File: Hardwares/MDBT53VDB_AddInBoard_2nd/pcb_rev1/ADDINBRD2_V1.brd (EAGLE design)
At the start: 25 x 31 mm, 21 parts, among them CN1 IF_4PIN, CN2 IF_4PIN, CN3 IF_2PIN, CN4 IF_2PIN, Q1 DMP2035UFDF-7, Q2 BC817-40QA, SW1 SKRPACE010, U1 SN74AHC1G00DRLR, U2 REF3325AIRSER, U3 MCP6232T-E/MNY

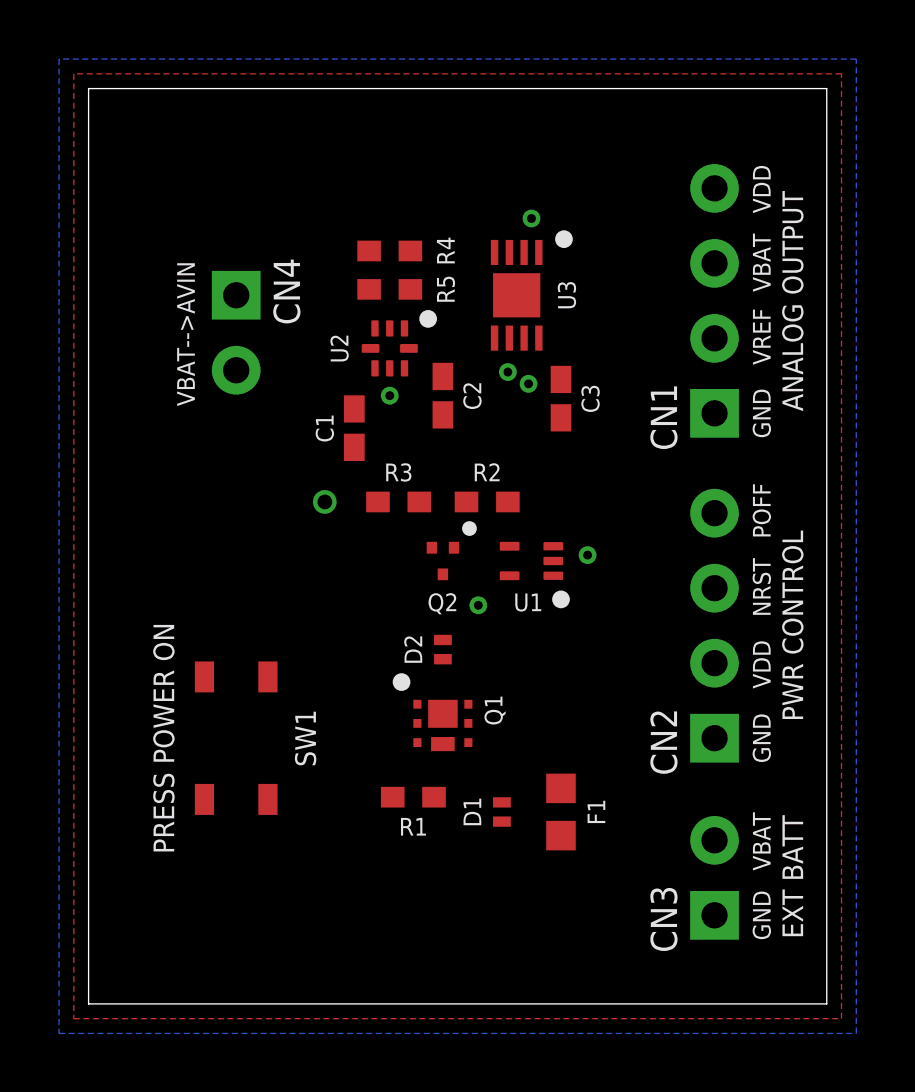
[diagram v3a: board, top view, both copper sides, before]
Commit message: レイアウトを修正
・MOSFET周りを配線
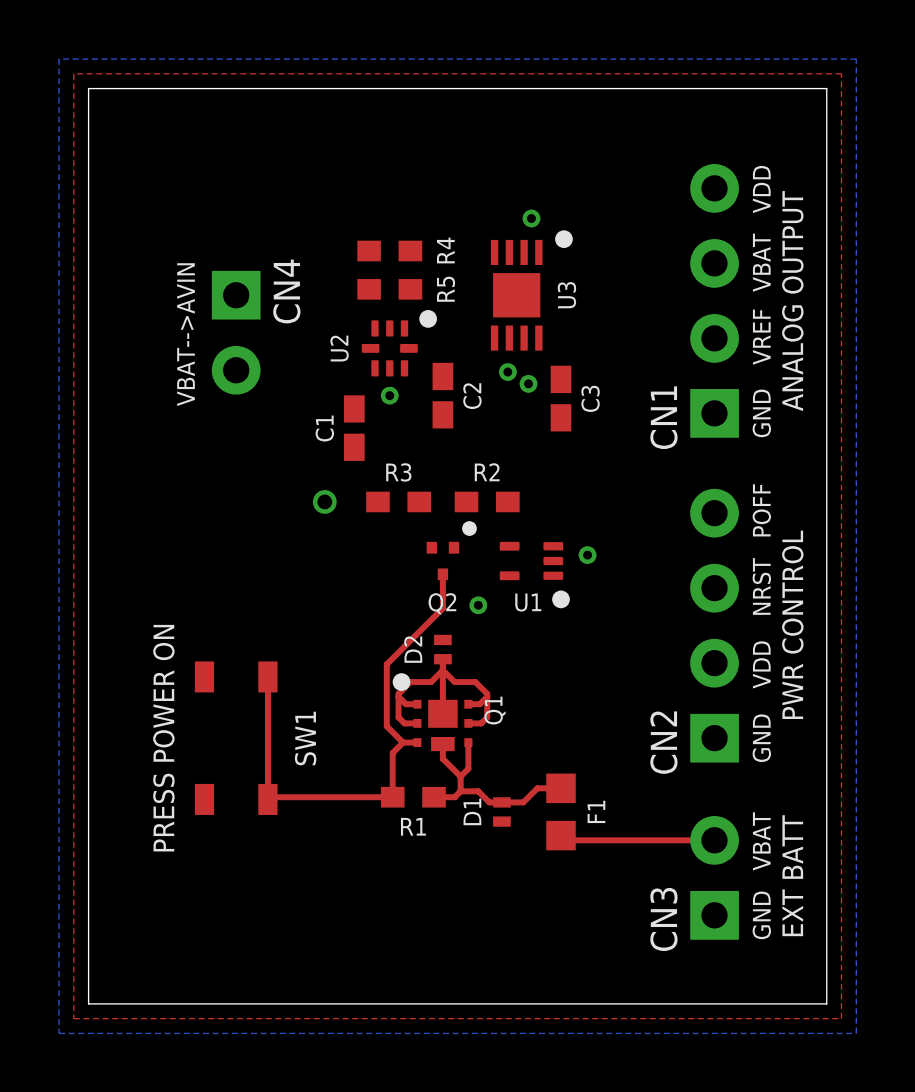
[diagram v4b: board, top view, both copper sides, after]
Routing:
- net PWR_G: track 0.00 -> 17.6 mm
- net N$2: track 0.00 -> 10.4 mm
- net N$1: track 0.00 -> 7.84 mm
- net EXT_BAT: track 0.00 -> 5.27 mm
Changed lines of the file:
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@@
 <contactref element="Q1" pad="EXP2"/>
 <contactref element="Q1" pad="4"/>
-<wire x1="14" y1="6.825" x2="16" y2="7.3" width="0" layer="19" extent="1-1"/>
-<wire x1="12.863" y1="8.85" x2="14" y2="6.825" width="0" layer="19" extent="1-1"/>
-<wire x1="12" y1="8.8" x2="12.863" y2="8.85" width="0" layer="19" extent="1-1"/>
-<wire x1="11.7" y1="7" x2="12" y2="8.8" width="0" layer="19" extent="1-1"/>
+<wire x1="14" y1="6.825" x2="14.725" y2="6.825" width="0.2032" layer="1"/>
+<wire x1="14.725" y1="6.825" x2="15.2" y2="7.3" width="0.2032" layer="1"/>
+<wire x1="16" y1="7.3" x2="15.2" y2="7.3" width="0.2032" layer="1"/>
+<wire x1="14" y1="6.825" x2="13.575" y2="6.825" width="0.2032" layer="1"/>
+<wire x1="12" y1="8.8" x2="12" y2="8.3" width="0.2032" layer="1"/>
+<wire x1="13.575" y1="6.825" x2="13.2" y2="7.2" width="0.2032" layer="1"/>
+<wire x1="13.2" y1="7.2" x2="12.6" y2="7.2" width="0.2032" layer="1"/>
+<wire x1="12.6" y1="7.2" x2="12.4" y2="7" width="0.2032" layer="1"/>
+<wire x1="12.4" y1="7" x2="11.7" y2="7" width="0.2032" layer="1"/>
+<wire x1="12" y1="8.3" x2="12.6" y2="7.7" width="0.2032" layer="1"/>
+<wire x1="12.6" y1="7.7" x2="12.6" y2="7.2" width="0.2032" layer="1"/>
+<wire x1="12.863" y1="8.85" x2="12.863" y2="7.963" width="0.2032" layer="1"/>
+<wire x1="12.863" y1="7.963" x2="12.6" y2="7.7" width="0.2032" layer="1"/>
 </signal>
 <signal name="PWR_G">
@@
 <contactref element="Q2" pad="3"/>
 <contactref element="Q1" pad="3"/>
-<wire x1="11.137" y1="8.85" x2="12" y2="14.55" width="0" layer="19" extent="1-1"/>
-<wire x1="10.3" y1="7" x2="11.137" y2="8.85" width="0" layer="19" extent="1-1"/>
-<wire x1="6.075" y1="6.925" x2="10.3" y2="7" width="0" layer="19" extent="1-1"/>
-<wire x1="6.075" y1="11.075" x2="6.075" y2="6.925" width="0" layer="19" extent="1-1"/>
+<wire x1="10.3" y1="7" x2="6.15" y2="7" width="0.2032" layer="1"/>
+<wire x1="6.15" y1="7" x2="6.075" y2="6.925" width="0.2032" layer="1"/>
+<wire x1="6.075" y1="11.075" x2="6.075" y2="6.925" width="0.2032" layer="1"/>
+<wire x1="11.137" y1="8.85" x2="10.65" y2="8.85" width="0.2032" layer="1"/>
+<wire x1="10.65" y1="8.85" x2="10.1" y2="9.4" width="0.2032" layer="1"/>
+<wire x1="10.1" y1="9.4" x2="10.1" y2="11.5" width="0.2032" layer="1"/>
+<wire x1="10.1" y1="11.5" x2="12" y2="13.4" width="0.2032" layer="1"/>
+<wire x1="12" y1="14.55" x2="12" y2="13.4" width="0.2032" layer="1"/>
+<wire x1="10.65" y1="8.85" x2="10.3" y2="8.5" width="0.2032" layer="1"/>
+<wire x1="10.3" y1="7" x2="10.3" y2="8.5" width="0.2032" layer="1"/>
 </signal>
 <signal name="VIN">
@@
 <contactref element="F1" pad="1"/>
 <contactref element="CN3" pad="2"/>
-<wire x1="16" y1="5.7" x2="21.2" y2="5.54" width="0" layer="19" extent="1-1"/>
+<wire x1="21.2" y1="5.54" x2="16.16" y2="5.54" width="0.2032" layer="1"/>
+<wire x1="16.16" y1="5.54" x2="16" y2="5.7" width="0.2032" layer="1"/>
 </signal>
 <signal name="N$5">
@@
 <contactref element="Q1" pad="2"/>
 <contactref element="D2" pad="1"/>
-<wire x1="12.863" y1="9.5" x2="12.863" y2="10.15" width="0" layer="19" extent="1-1"/>
-<wire x1="12" y1="9.825" x2="12.863" y2="10.15" width="0" layer="19" extent="1-1"/>
-<wire x1="11.137" y1="10.15" x2="12" y2="9.825" width="0" layer="19" extent="1-1"/>
-<wire x1="11.137" y1="9.5" x2="11.137" y2="10.15" width="0" layer="19" extent="1-1"/>
-<wire x1="12" y1="11.675" x2="12.863" y2="10.15" width="0" layer="19" extent="1-1"/>
+<wire x1="12.863" y1="10.15" x2="13.25" y2="10.15" width="0.2032" layer="1"/>
+<wire x1="12.863" y1="9.5" x2="13.3" y2="9.5" width="0.2032" layer="1"/>
+<wire x1="13.3" y1="9.5" x2="13.5" y2="9.7" width="0.2032" layer="1"/>
+<wire x1="13.5" y1="9.7" x2="13.5" y2="10.4" width="0.2032" layer="1"/>
+<wire x1="13.25" y1="10.15" x2="13.5" y2="10.4" width="0.2032" layer="1"/>
+<wire x1="11.137" y1="9.5" x2="10.7" y2="9.5" width="0.2032" layer="1"/>
+<wire x1="10.7" y1="9.5" x2="10.5" y2="9.7" width="0.2032" layer="1"/>
+<wire x1="10.5" y1="9.7" x2="10.5" y2="10.4" width="0.2032" layer="1"/>
+<wire x1="11.137" y1="10.15" x2="10.75" y2="10.15" width="0.2032" layer="1"/>
+<wire x1="10.75" y1="10.15" x2="10.5" y2="10.4" width="0.2032" layer="1"/>
+<wire x1="12" y1="11.3" x2="12.4" y2="10.9" width="0.2032" layer="1"/>
+<wire x1="12.4" y1="10.9" x2="13.1" y2="10.9" width="0.2032" layer="1"/>
+<wire x1="12" y1="11.3" x2="11.6" y2="10.9" width="0.2032" layer="1"/>
+<wire x1="11.6" y1="10.9" x2="10.9" y2="10.9" width="0.2032" layer="1"/>
+<wire x1="12" y1="11.3" x2="12" y2="11.675" width="0.2032" layer="1"/>
+<wire x1="10.9" y1="10.9" x2="10.5" y2="10.5" width="0.2032" layer="1"/>
+<wire x1="10.5" y1="10.5" x2="10.5" y2="10.4" width="0.2032" layer="1"/>
+<wire x1="13.1" y1="10.9" x2="13.5" y2="10.5" width="0.2032" layer="1"/>
+<wire x1="13.5" y1="10.5" x2="13.5" y2="10.4" width="0.2032" layer="1"/>
+<wire x1="12" y1="9.825" x2="12" y2="11.675" width="0.2032" layer="1"/>
 </signal>
 <signal name="N$3">

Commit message: レイアウトを修正
・ロジックIC周りを配線
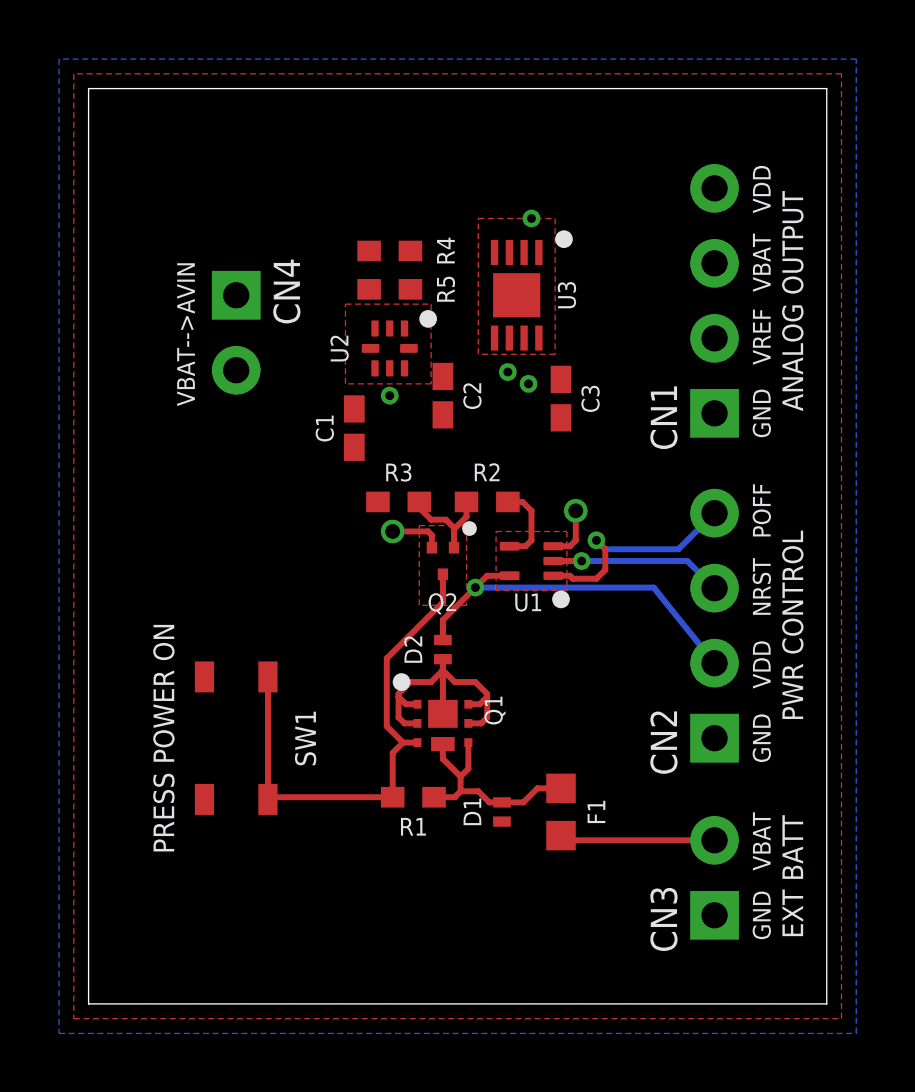
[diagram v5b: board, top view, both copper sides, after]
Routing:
- net VIN: track 0.00 -> 13.4 mm
- net PWR_OFF: track 0.00 -> 7.68 mm, vias 0 -> 1
- net NRST: track 0.00 -> 5.84 mm
- net 0V: track 0.00 -> 3.64 mm, vias 1 -> 2
- net N$5: track 0.00 -> 3.43 mm
- net N$3: track 0.00 -> 2.75 mm
- added copper zone on layer 1, net N$4
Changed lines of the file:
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@@
 <contactref element="SW1" pad="1"/>
 <contactref element="SW1" pad="2"/>
-<via x="8" y="17" extent="1-16" drill="0.5"/>
+<via x="16.5" y="16.7" extent="1-16" drill="0.5"/>
 <contactref element="U2" pad="4"/>
 <contactref element="C1" pad="2"/>
@@
 <contactref element="CN3" pad="1"/>
 <contactref element="CN2" pad="1"/>
+<wire x1="15.74" y1="15.5" x2="16.3" y2="15.5" width="0.2032" layer="1"/>
+<wire x1="16.3" y1="15.5" x2="16.5" y2="15.7" width="0.2032" layer="1"/>
+<wire x1="16.5" y1="16.7" x2="16.5" y2="15.7" width="0.2032" layer="1"/>
+<via x="10.3" y="16" extent="1-16" drill="0.5"/>
+<wire x1="11.625" y1="15.45" x2="11.625" y2="15.875" width="0.2032" layer="1"/>
+<wire x1="11.625" y1="15.875" x2="11.5" y2="16" width="0.2032" layer="1"/>
+<wire x1="10.3" y1="16" x2="11.5" y2="16" width="0.2032" layer="1"/>
 <wire x1="14.5" y1="24" x2="13.75" y2="25.45" width="0" layer="19" extent="1-1"/>
+<wire x1="9.5" y1="25.5" x2="13.75" y2="25.45" width="0" layer="19" extent="1-1"/>
 <wire x1="9.55" y1="22.2" x2="9.5" y2="25.5" width="0" layer="19" extent="1-1"/>
-<wire x1="15.74" y1="15.5" x2="11.625" y2="15.45" width="0" layer="19" extent="1-1"/>
 </signal>
 <signal name="N$1">
@@
 <wire x1="11.137" y1="8.85" x2="10.65" y2="8.85" width="0.2032" layer="1"/>
 <wire x1="10.65" y1="8.85" x2="10.1" y2="9.4" width="0.2032" layer="1"/>
-<wire x1="10.1" y1="9.4" x2="10.1" y2="11.5" width="0.2032" layer="1"/>
-<wire x1="10.1" y1="11.5" x2="12" y2="13.4" width="0.2032" layer="1"/>
-<wire x1="12" y1="14.55" x2="12" y2="13.4" width="0.2032" layer="1"/>
+<wire x1="10.1" y1="9.4" x2="10.1" y2="11.7" width="0.2032" layer="1"/>
 <wire x1="10.65" y1="8.85" x2="10.3" y2="8.5" width="0.2032" layer="1"/>
 <wire x1="10.3" y1="7" x2="10.3" y2="8.5" width="0.2032" layer="1"/>
+<wire x1="10.1" y1="11.7" x2="12" y2="13.6" width="0.2032" layer="1"/>
+<wire x1="12" y1="13.6" x2="12" y2="14.55" width="0.2032" layer="1"/>
 </signal>
 <signal name="VIN">
@@
 <contactref element="CN2" pad="2"/>
 <contactref element="CN4" pad="2"/>
-<via x="13.2" y="13.5" extent="1-16" drill="0.3"/>
-<wire x1="14.26" y1="14.5" x2="21.2" y2="11.54" width="0" layer="19" extent="1-1"/>
-<wire x1="13.2" y1="13.5" x2="14.26" y2="14.5" width="0" layer="19" extent="1-1"/>
-<wire x1="12" y1="12.325" x2="13.2" y2="13.5" width="0" layer="19" extent="1-1"/>
-<wire x1="5" y1="21.46" x2="13.2" y2="13.5" width="0" layer="19" extent="1-1"/>
+<via x="13.1" y="14.1" extent="1-16" drill="0.3"/>
+<wire x1="21.2" y1="11.54" x2="19.14" y2="14.1" width="0.2032" layer="16"/>
+<wire x1="19.14" y1="14.1" x2="13.1" y2="14.1" width="0.2032" layer="16"/>
+<wire x1="14.26" y1="14.5" x2="13.5" y2="14.5" width="0.2032" layer="1"/>
+<wire x1="13.5" y1="14.5" x2="13.1" y2="14.1" width="0.2032" layer="1"/>
+<wire x1="12" y1="12.325" x2="12" y2="12.8" width="0.2032" layer="1"/>
+<wire x1="13.1" y1="14.1" x2="12" y2="13" width="0.2032" layer="1"/>
+<wire x1="12" y1="13" x2="12" y2="12.325" width="0.2032" layer="1"/>
+<wire x1="13.1" y1="14.1" x2="5" y2="21.46" width="0" layer="19" extent="16-16"/>
 </signal>
 <signal name="EXT_BAT">
 <contactref element="F1" pad="1"/>
 <contactref element="CN3" pad="2"/>
+<wire x1="16.3" y1="5.4" x2="16" y2="5.7" width="0.2032" layer="1"/>
 <wire x1="21.2" y1="5.54" x2="16.16" y2="5.54" width="0.2032" layer="1"/>
 <wire x1="16.16" y1="5.54" x2="16" y2="5.7" width="0.2032" layer="1"/>
@@
 <contactref element="R3" pad="2"/>
 <contactref element="Q2" pad="1"/>
-<wire x1="11.2" y1="17" x2="12.8" y2="17" width="0" layer="19" extent="1-1"/>
-<wire x1="12.375" y1="15.45" x2="12.8" y2="17" width="0" layer="19" extent="1-1"/>
+<wire x1="12.375" y1="15.45" x2="12.375" y2="16.075" width="0.2032" layer="1"/>
+<wire x1="12.375" y1="16.075" x2="12.8" y2="16.5" width="0.2032" layer="1"/>
+<wire x1="12.8" y1="17" x2="12.8" y2="16.5" width="0.2032" layer="1"/>
+<wire x1="12.375" y1="16.075" x2="12.375" y2="16.125" width="0.2032" layer="1"/>
+<wire x1="12.375" y1="16.125" x2="12.1" y2="16.4" width="0.2032" layer="1"/>
+<wire x1="12.1" y1="16.4" x2="11.6" y2="16.4" width="0.2032" layer="1"/>
+<wire x1="11.2" y1="17" x2="11.2" y2="16.8" width="0.2032" layer="1"/>
+<wire x1="11.2" y1="16.8" x2="11.6" y2="16.4" width="0.2032" layer="1"/>
 </signal>
 <signal name="AVREF_IN">
@@
 <contactref element="U1" pad="4"/>
 <contactref element="R2" pad="1"/>
-<wire x1="14.2" y1="17" x2="14.26" y2="15.5" width="0" layer="19" extent="1-1"/>
+<wire x1="14.26" y1="15.5" x2="14.8" y2="15.5" width="0.2032" layer="1"/>
+<wire x1="14.8" y1="15.5" x2="15" y2="15.7" width="0.2032" layer="1"/>
+<wire x1="15" y1="15.7" x2="15" y2="16.7" width="0.2032" layer="1"/>
+<wire x1="14.2" y1="17" x2="14.7" y2="17" width="0.2032" layer="1"/>
+<wire x1="14.7" y1="17" x2="15" y2="16.7" width="0.2032" layer="1"/>
 </signal>
 <signal name="NRST">
 <contactref element="U1" pad="2"/>
 <contactref element="CN2" pad="3"/>
-<via x="16.9" y="15.2" extent="1-16" drill="0.3"/>
-<wire x1="16.9" y1="15.2" x2="21.2" y2="14.08" width="0" layer="19" extent="1-1"/>
-<wire x1="15.74" y1="15" x2="16.9" y2="15.2" width="0" layer="19" extent="1-1"/>
+<via x="16.7" y="15" extent="1-16" drill="0.3"/>
+<wire x1="16.7" y1="15" x2="20.28" y2="15" width="0.2032" layer="16"/>
+<wire x1="20.28" y1="15" x2="21.2" y2="14.08" width="0.2032" layer="16"/>
+<wire x1="15.74" y1="15" x2="16.7" y2="15" width="0.2032" layer="1"/>
 </signal>
 <signal name="PWR_OFF">
 <contactref element="U1" pad="1"/>
 <contactref element="CN2" pad="4"/>
-<wire x1="15.74" y1="14.5" x2="21.2" y2="16.62" width="0" layer="19" extent="1-1"/>
+<via x="17.2" y="15.7" extent="1-16" drill="0.3"/>
+<wire x1="19.98" y1="15.4" x2="21.2" y2="16.62" width="0.2032" layer="16"/>
+<wire x1="15.74" y1="14.5" x2="16.3" y2="14.5" width="0.2032" layer="1"/>
+<wire x1="16.3" y1="14.5" x2="16.4" y2="14.4" width="0.2032" layer="1"/>
+<wire x1="16.4" y1="14.4" x2="17.2" y2="14.4" width="0.2032" layer="1"/>
+<wire x1="17.2" y1="14.4" x2="17.5" y2="14.7" width="0.2032" layer="1"/>
+<wire x1="17.5" y1="14.7" x2="17.5" y2="15.4" width="0.2032" layer="1"/>
+<wire x1="17.2" y1="15.7" x2="17.5" y2="15.4" width="0.2032" layer="1"/>
+<wire x1="19.98" y1="15.4" x2="17.5" y2="15.4" width="0.2032" layer="16"/>
+<wire x1="17.5" y1="15.4" x2="17.2" y2="15.7" width="0.2032" layer="16"/>
 </signal>
 <signal name="AVBAT">
@@
 <wire x1="5" y1="24" x2="9.5" y2="24.2" width="0" layer="19" extent="1-1"/>
 </signal>
+<signal name="N$4">
+<polygon width="0" layer="1" pour="cutout" isolate="0.2032">
+<vertex x="13.8" y="16"/>
+<vertex x="16.2" y="16"/>
+<vertex x="16.2" y="14"/>
+<vertex x="13.8" y="14"/>
+</polygon>
+<polygon width="0" layer="1" pour="cutout" isolate="0.2032">
+<vertex x="11.2" y="16.2"/>
+<vertex x="12.8" y="16.2"/>
+<vertex x="12.8" y="13.5"/>
+<vertex x="11.2" y="13.5"/>
+</polygon>
+<polygon width="0" layer="1" pour="cutout" isolate="0.2032">
+<vertex x="8.7" y="23.7"/>
+<vertex x="11.6" y="23.7"/>
+<vertex x="11.6" y="21"/>
+<vertex x="8.7" y="21"/>
+</polygon>
+<polygon width="0" layer="1" pour="cutout" isolate="0.2032">
+<vertex x="13.2" y="26.6"/>
+<vertex x="15.8" y="26.6"/>
+<vertex x="15.8" y="22"/>
+<vertex x="13.2" y="22"/>
+</polygon>
+</signal>
 </signals>

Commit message: レイアウトを修正
・VBAT-->AVIN（設定ジャンパー）周りを配線
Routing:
- net VIN: track 13.4 -> 26.6 mm, vias 1 -> 2
- net AVIN: track 0.00 -> 7.12 mm
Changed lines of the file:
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@@
 <wire x1="13.1" y1="14.1" x2="12" y2="13" width="0.2032" layer="1"/>
 <wire x1="12" y1="13" x2="12" y2="12.325" width="0.2032" layer="1"/>
-<wire x1="13.1" y1="14.1" x2="5" y2="21.46" width="0" layer="19" extent="16-16"/>
+<via x="12" y="18" extent="1-16" drill="0.3"/>
+<wire x1="13.5" y1="14.5" x2="13.5" y2="17.7" width="0.2032" layer="1"/>
+<wire x1="13.5" y1="17.7" x2="13.2" y2="18" width="0.2032" layer="1"/>
+<wire x1="13.2" y1="18" x2="12" y2="18" width="0.2032" layer="1"/>
+<wire x1="5" y1="21.46" x2="6.24" y2="21.46" width="0.2032" layer="16"/>
+<wire x1="6.24" y1="21.46" x2="7.6" y2="20.1" width="0.2032" layer="16"/>
+<wire x1="7.6" y1="20.1" x2="9.9" y2="20.1" width="0.2032" layer="16"/>
+<wire x1="9.9" y1="20.1" x2="12" y2="18" width="0.2032" layer="16"/>
 </signal>
 <signal name="EXT_BAT">
@@
 <contactref element="CN4" pad="1"/>
 <via x="14.9" y="21" extent="1-16" drill="0.3"/>
-<via x="10.2" y="20.6" extent="1-16" drill="0.3"/>
+<via x="10.3" y="20.6" extent="1-16" drill="0.3"/>
+<wire x1="5" y1="24" x2="5" y2="23.3" width="0.2032" layer="16"/>
+<wire x1="7.7" y1="20.6" x2="10.3" y2="20.6" width="0.2032" layer="16"/>
+<wire x1="5" y1="23.3" x2="7.7" y2="20.6" width="0.2032" layer="16"/>
 <wire x1="15.25" y1="22.55" x2="21.2" y2="27.62" width="0" layer="19" extent="1-1"/>
 <wire x1="16" y1="21.15" x2="15.25" y2="22.55" width="0" layer="19" extent="1-1"/>
 <wire x1="14.9" y1="21" x2="16" y2="21.15" width="0" layer="19" extent="1-1"/>
-<wire x1="10.2" y1="20.6" x2="14.9" y2="21" width="0" layer="19" extent="1-1"/>
-<wire x1="9.7" y1="21.525" x2="10.2" y2="20.6" width="0" layer="19" extent="1-1"/>
-<wire x1="9" y1="20.15" x2="10.2" y2="20.6" width="0" layer="19" extent="1-1"/>
+<wire x1="10.3" y1="20.6" x2="14.9" y2="21" width="0" layer="19" extent="1-1"/>
+<wire x1="9.7" y1="21.525" x2="10.3" y2="20.6" width="0" layer="19" extent="1-1"/>
+<wire x1="9" y1="20.15" x2="10.3" y2="20.6" width="0" layer="19" extent="1-1"/>
 <wire x1="9.5" y1="24.2" x2="9.7" y2="21.525" width="0" layer="19" extent="1-1"/>
-<wire x1="5" y1="24" x2="9.5" y2="24.2" width="0" layer="19" extent="1-1"/>
 </signal>
 <signal name="N$4">
